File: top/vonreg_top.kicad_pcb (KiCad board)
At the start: 2 copper layers, 111 x 97 mm, 17 parts, among them K1 SW_Push, K10 SW_Push, K11 SW_Push, K12 SW_Push, K15 SW_Push, K2 SW_Push, K3 SW_Push, K4 SW_Push, K5 SW_Push, K6 SW_Push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

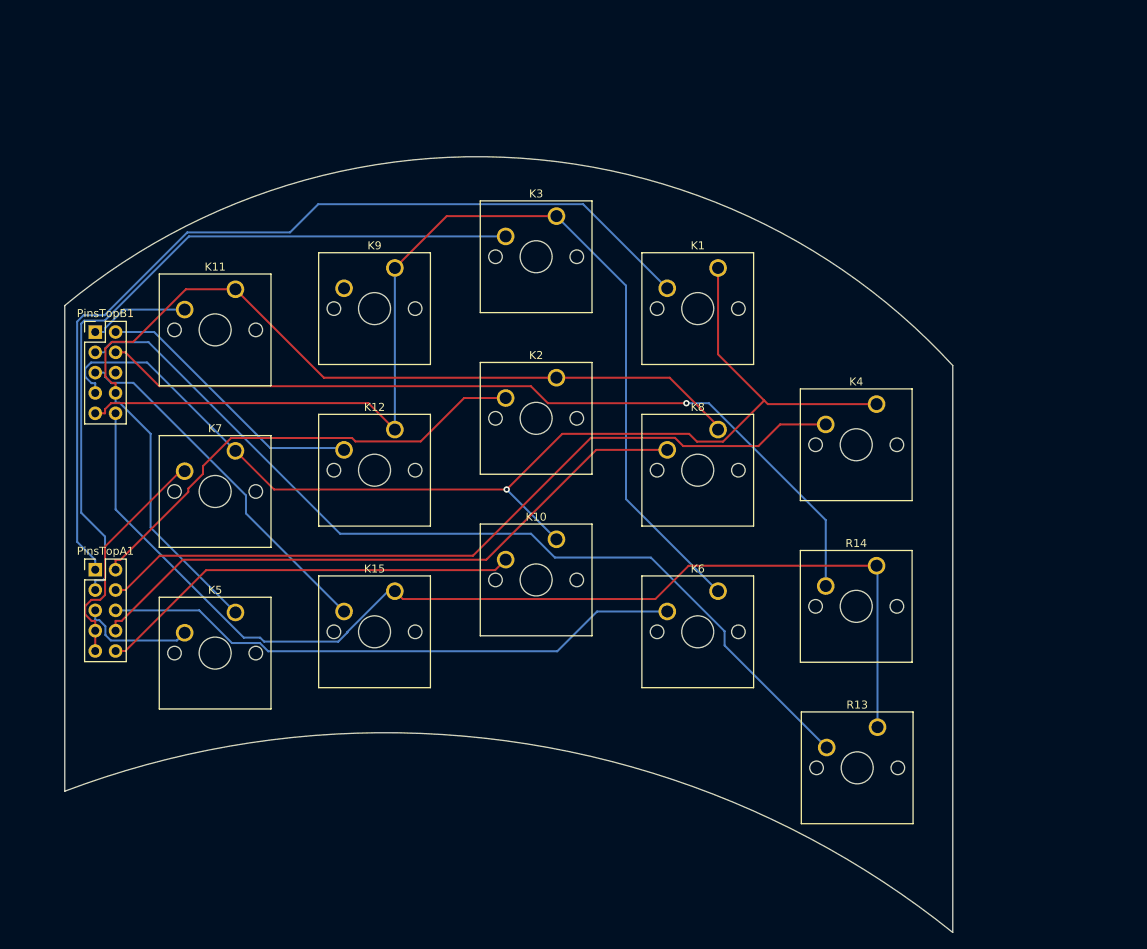
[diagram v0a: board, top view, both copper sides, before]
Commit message: Aligned top/bottom
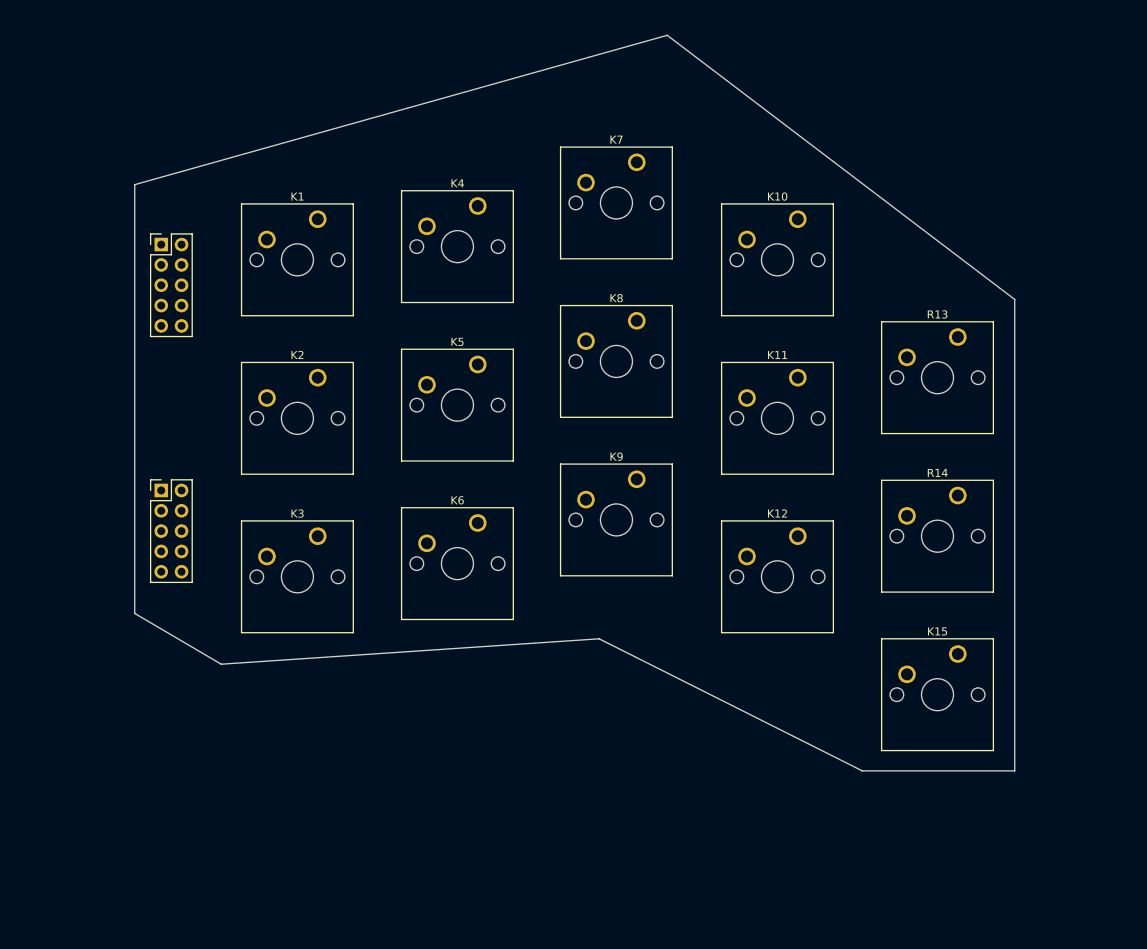
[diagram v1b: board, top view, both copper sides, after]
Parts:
- removed PinsTopA1, PinsTopB1: Conn_02x05_Odd_Even, Connector_PinHeader_2.54mm:PinHeader_2x05_P2.54mm_Vertical
- added ?: Conn_02x05_Odd_Even, Connector_PinHeader_2.54mm:PinHeader_2x05_P2.54mm_Vertical, F.Cu at (67.8, 59.4)
- added ?: Conn_02x05_Odd_Even, Connector_PinHeader_2.54mm:PinHeader_2x05_P2.54mm_Vertical, F.Cu at (67.8, 90.2)
- moved K11 71.2 mm to (147.4, 76.1)
- moved K15 70.8 mm to (167.4, 110.6)
- moved K7 61.8 mm to (127.3, 49.1)
- moved K4 55.7 mm to (107.4, 54.6)
- moved K12 52.1 mm to (147.4, 95.9)
- moved K1 50.4 mm to (87.4, 56.3)
- moved K10 50.1 mm to (147.4, 56.3)
- moved K3 49.9 mm to (87.4, 95.9)
- moved R13 49.8 mm to (167.4, 71.0)
- moved K5 43.3 mm to (107.4, 74.4)
- moved K9 40.2 mm to (127.3, 88.8)
- moved K6 31.2 mm to (107.4, 94.2)
- moved K2 29.8 mm to (87.4, 76.1)
- moved K8 17.0 mm to (127.3, 69.0)
- moved R14 13.4 mm to (167.4, 90.8)
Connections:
- K1 pad 1: /C1 -> GND
- K10 pad 1: /C1 -> GND
- K11 pad 1: /C2 -> GND
- K12 pad 1: /C3 -> GND
- K15 pad 1: /C4 -> GND
- K2 pad 1: /C2 -> GND
- K3 pad 1: /C3 -> GND
- K4 pad 1: /C1 -> GND
- K5 pad 1: /C2 -> GND
- K6 pad 1: /C3 -> GND
- K7 pad 1: /C1 -> GND
- K8 pad 1: /C2 -> GND
- K9 pad 1: /C3 -> GND
- R13 pad 1: /C4 -> GND
- R14 pad 1: /C4 -> GND
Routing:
- net /C1: track 143.0 -> 0.00 mm, vias 1 -> 0
- net /C4: track 139.0 -> 0.00 mm
- net /C3: track 138.0 -> 0.00 mm
- net /C2: track 127.5 -> 0.00 mm
- net /RT1: track 116.1 -> 0.00 mm
- net /RT13: track 114.3 -> 0.00 mm
- net /RT14: track 105.7 -> 0.00 mm, vias 1 -> 0
- net /RT4: track 98.2 -> 0.00 mm
- net /RT3: track 93.2 -> 0.00 mm
- net /RT8: track 79.0 -> 0.00 mm
- net /RT6: track 73.1 -> 0.00 mm
- net /RT2: track 59.5 -> 0.00 mm
- net /RT10: track 53.5 -> 0.00 mm
- net /RT15: track 45.1 -> 0.00 mm
- net /RT12: track 34.7 -> 0.00 mm
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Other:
- board size 111 x 97 mm -> 110 x 91.9 mm

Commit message: Routing done, hopefully
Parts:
- K1, K10, K11, K12, K15, K2, K3, K4, K5, K6, K7, K8, K9, R13, R14: footprint Button_Switch_Keyboard:SW_Cherry_MX_1.00u_PCB -> Button_Switch_Keyboard:Kailh_socket_MX_optional_reversible
- moved PinsTopA1 30.7 mm to (67.8, 59.4)
- moved PinsTopB1 30.7 mm to (67.8, 90.2)
- moved K11 5.18 mm to (144.3, 80.3)
- moved K15 5.18 mm to (164.3, 114.8)
- moved K2 5.18 mm to (84.3, 80.3)
- moved K4 5.18 mm to (104.3, 58.8)
- moved K5 5.18 mm to (104.3, 78.6)
- moved K6 5.18 mm to (104.3, 98.4)
- moved K7 5.18 mm to (124.2, 53.3)
- moved K8 5.18 mm to (124.2, 73.2)
- moved K9 5.18 mm to (124.2, 93.0)
- moved R13 5.18 mm to (164.3, 75.2)
- moved K1 5.18 mm to (84.3, 60.5)
- moved K10 5.18 mm to (144.3, 60.5)
- moved K12 5.18 mm to (144.3, 100.1)
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- gave numbers to parts that had none: 2
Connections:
- PinsTopA1 pad 1: /RT1 -> unconnected-(PinsTopA1-Pad1)
- PinsTopA1 pad 10: /RT10 -> /RT7
- PinsTopA1 pad 2: /RT2 -> /RT14
- PinsTopA1 pad 3: /RT3 -> unconnected-(PinsTopA1-Pad3)
- PinsTopA1 pad 4: /RT4 -> /RT13
- PinsTopA1 pad 5: /RT5 -> unconnected-(PinsTopA1-Pad5)
- PinsTopA1 pad 6: /RT6 -> /RT1
- PinsTopA1 pad 7: /RT7 -> unconnected-(PinsTopA1-Pad7)
- PinsTopA1 pad 8: /RT8 -> /RT4
- PinsTopA1 pad 9: /RT7 -> /RT10
- PinsTopB1 pad 1: /RT11 -> /RT8
- PinsTopB1 pad 10: GND -> /RT9
- PinsTopB1 pad 2: /RT12 -> /RT11
- PinsTopB1 pad 3: /RT13 -> /RT5
- PinsTopB1 pad 4: /RT14 -> GND
- PinsTopB1 pad 5: /RT15 -> /RT2
- PinsTopB1 pad 6: unconnected-(PinsTopB1-Pad6) -> /RT3
- PinsTopB1 pad 7: unconnected-(PinsTopB1-Pad7) -> /RT15
- PinsTopB1 pad 8: unconnected-(PinsTopB1-Pad8) -> /RT6
- PinsTopB1 pad 9: unconnected-(PinsTopB1-Pad9) -> /RT12
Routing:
- net GND: track 0.00 -> 515.2 mm
- net /RT14: track 0.00 -> 180.6 mm
- net /RT15: track 0.00 -> 156.0 mm
- net /RT13: track 0.00 -> 154.0 mm
- net /RT12: track 0.00 -> 121.5 mm
- net /RT10: track 0.00 -> 117.7 mm
- net /RT11: track 0.00 -> 116.2 mm
- net /RT8: track 0.00 -> 99.5 mm
- net /RT9: track 0.00 -> 98.0 mm
- net /RT7: track 0.00 -> 94.4 mm
- net /RT5: track 0.00 -> 82.1 mm
- net /RT6: track 0.00 -> 76.8 mm
- net /RT4: track 0.00 -> 71.9 mm
- net /RT2: track 0.00 -> 66.6 mm
- net /RT3: track 0.00 -> 59.5 mm
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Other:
- outline, holes or cut-outs redrawn

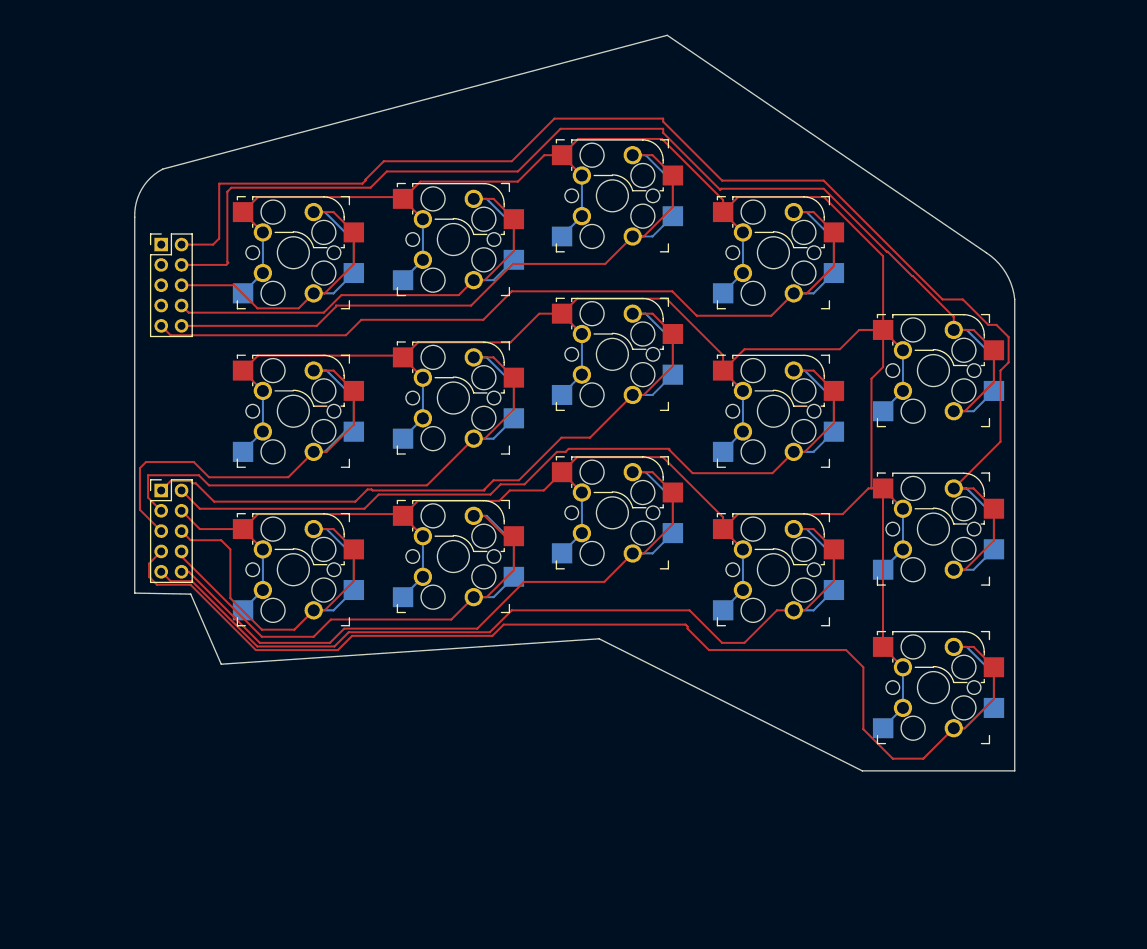
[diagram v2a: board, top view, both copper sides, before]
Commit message: Rounded edge cuts
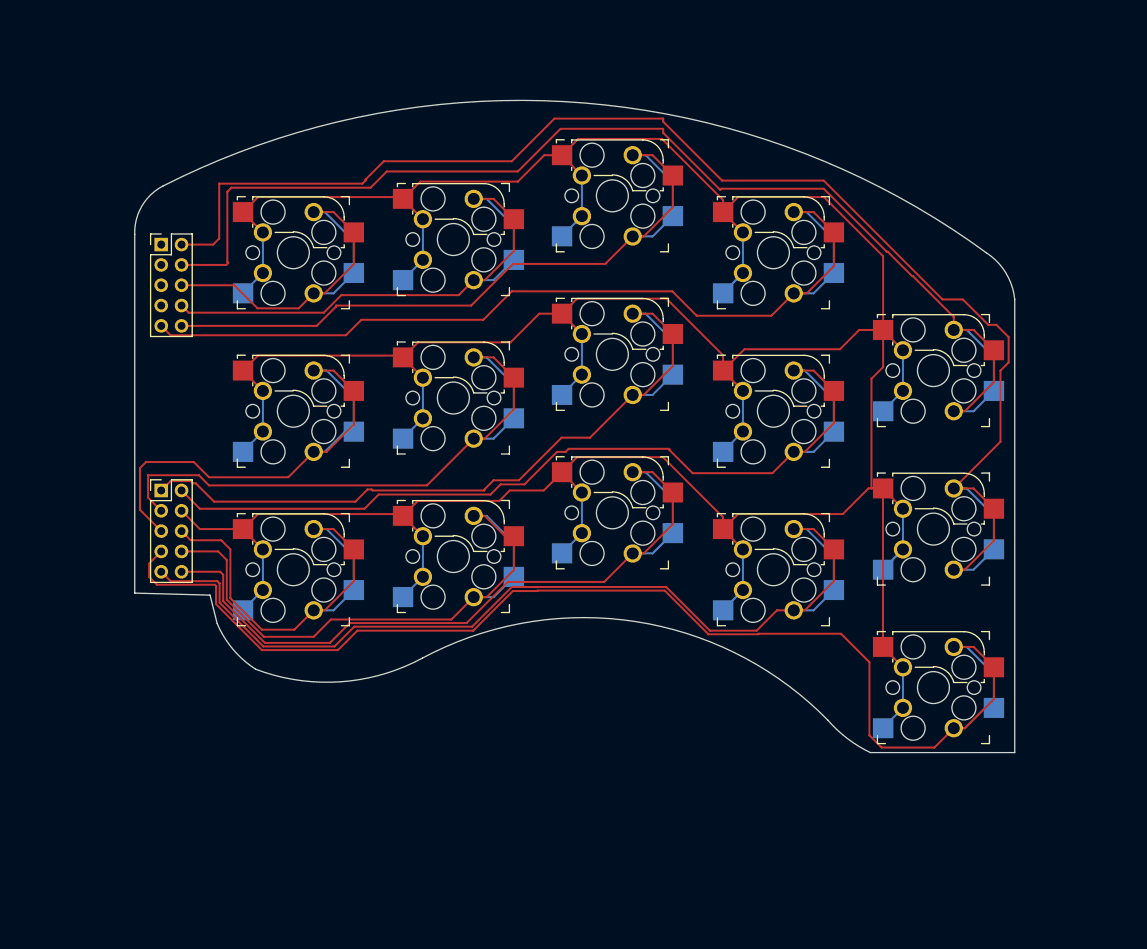
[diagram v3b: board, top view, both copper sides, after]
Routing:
- net /RT15: track 156.0 -> 160.4 mm
- net /RT12: track 121.5 -> 124.0 mm
- net /RT6: track 76.8 -> 79.3 mm
- net /RT9: track 98.0 -> 99.9 mm
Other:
- board size 110 x 91.9 mm -> 110 x 81.5 mm

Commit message: Ground pour and buzzer
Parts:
- added HOLE1: MountingHole_2.5mm_Pad, MountingHole:MountingHole_2.5mm_Pad, F.Cu at (136.1, 70.6)
- added HOLE1: MountingHole_2.5mm_Pad, MountingHole:MountingHole_2.5mm_Pad, F.Cu at (136.0, 90.7)
- added HOLE1: MountingHole_2.5mm_Pad, MountingHole:MountingHole_2.5mm_Pad, F.Cu at (153.8, 89.0)
- added HOLE1: MountingHole_2.5mm_Pad, MountingHole:MountingHole_2.5mm_Pad, F.Cu at (94.0, 73.2)
- added HOLE1: MountingHole_2.5mm_Pad, MountingHole:MountingHole_2.5mm_Pad, F.Cu at (93.9, 93.5)
- added M1: MountingHole_2mm, MountingHole:MountingHole_2mm, F.Cu at (113.4, 88.5)
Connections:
- PinsTopA1 pad 1: unconnected-(PinsTopA1-Pad1) -> GND
- PinsTopA1 pad 10: /RT7 -> /RT11
- PinsTopA1 pad 2: /RT14 -> /RT1
- PinsTopA1 pad 4: /RT13 -> /RT4
- PinsTopA1 pad 6: /RT1 -> /RT7
- PinsTopA1 pad 7: unconnected-(PinsTopA1-Pad7) -> /RT10
- PinsTopA1 pad 8: /RT4 -> /RT13
- PinsTopA1 pad 9: /RT10 -> /RT14
- PinsTopB1 pad 1: /RT8 -> /RT2
- PinsTopB1 pad 10: /RT9 -> /RT3
- PinsTopB1 pad 2: /RT11 -> /RT5
- PinsTopB1 pad 3: /RT5 -> /RT8
- PinsTopB1 pad 4: GND -> /RT15
- PinsTopB1 pad 5: /RT2 -> unconnected-(PinsTopB1-Pad5)
- PinsTopB1 pad 6: /RT3 -> /RT12
- PinsTopB1 pad 7: /RT15 -> /RT9
- PinsTopB1 pad 9: /RT12 -> unconnected-(PinsTopB1-Pad9)
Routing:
- net GND: track 515.2 -> 58.6 mm
- net /RT14: track 180.6 -> 151.1 mm
- net /RT13: track 154.0 -> 136.4 mm
- net /RT15: track 160.4 -> 147.3 mm
- net /RT2: track 66.6 -> 54.2 mm
- net /RT5: track 82.1 -> 72.5 mm
- net /RT6: track 79.3 -> 74.3 mm
- net /RT12: track 124.0 -> 120.2 mm
- net /RT3: track 59.5 -> 56.4 mm
- net /RT1: track 51.6 -> 53.9 mm
- net /RT4: track 71.9 -> 74.0 mm
- net /RT10: track 117.7 -> 119.6 mm
- net /RT8: track 99.5 -> 98.2 mm
- net /RT7: track 94.4 -> 95.4 mm
- net /RT11: track 116.2 -> 117.1 mm
- added copper zone on B.Cu, net GND
